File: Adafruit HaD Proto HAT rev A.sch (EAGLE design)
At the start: 9 parts, among them U1 CAT24C32

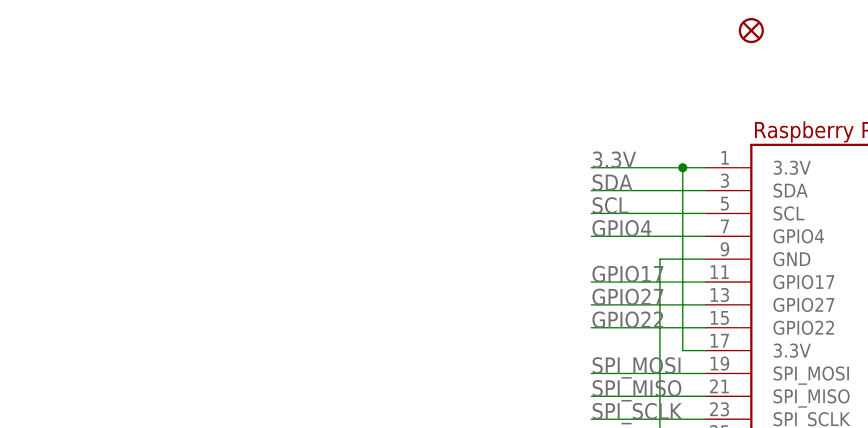
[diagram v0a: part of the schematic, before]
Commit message: ripped out proto area, added in 4xSAO connectors
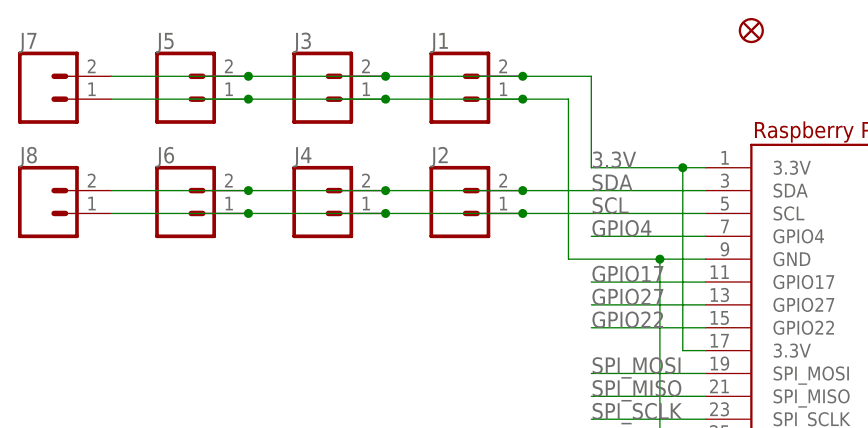
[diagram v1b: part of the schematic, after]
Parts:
- added J1, J2, J3, J4, J5, J6, J7, J8: (no value), SparkFun-Connectors:CONN_02LOCK
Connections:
- net 3.3V: now also J1.2, J3.2, J5.2, J7.2
- net GND: now also J1.1, J3.1, J5.1, J7.1
- net SCL: now also J2.1, J4.1, J6.1, J8.1
- net SDA: now also J2.2, J4.2, J6.2, J8.2
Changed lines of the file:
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@@
 <?xml version="1.0" encoding="utf-8"?>
 <!DOCTYPE eagle SYSTEM "eagle.dtd">
-<eagle version="6.3">
+<eagle version="9.0.1">
 <drawing>
 <settings>
 <setting alwaysvectorfont="no"/>
+<setting keepoldvectorfont="yes"/>
 <setting verticaltext="up"/>
 </settings>
@@
 <layer number="56" name="wert" color="7" fill="1" visible="no" active="no"/>
 <layer number="57" name="tCAD" color="7" fill="1" visible="no" active="no"/>
+<layer number="59" name="tCarbon" color="7" fill="1" visible="no" active="no"/>
+<layer number="60" name="bCarbon" color="7" fill="1" visible="no" active="no"/>
+<layer number="88" name="SimResults" color="9" fill="1" visible="no" active="yes"/>
+<layer number="89" name="SimProbes" color="9" fill="1" visible="no" active="yes"/>
+<layer number="90" name="Modules" color="5" fill="1" visible="yes" active="yes"/>
 <layer number="91" name="Nets" color="2" fill="1" visible="yes" active="yes"/>
 <layer number="92" name="Busses" color="1" fill="1" visible="yes" active="yes"/>
@@
 <layer number="97" name="Info" color="7" fill="1" visible="yes" active="yes"/>
 <layer number="98" name="Guide" color="6" fill="1" visible="yes" active="yes"/>
+<layer number="99" name="SpiceOrder" color="7" fill="1" visible="yes" active="yes"/>
 <layer number="100" name="Muster" color="7" fill="1" visible="no" active="yes"/>
 <layer number="101" name="Patch_Top" color="12" fill="4" visible="no" active="yes"/>
@@
 <layer number="111" name="MPL" color="7" fill="1" visible="no" active="yes"/>
 <layer number="112" name="tSilk" color="7" fill="1" visible="no" active="yes"/>
+<layer number="113" name="IDFDebug" color="4" fill="1" visible="no" active="no"/>
+<layer number="114" name="Badge_Outline" color="7" fill="1" visible="no" active="no"/>
+<layer number="115" name="ReferenceISLANDS" color="7" fill="1" visible="no" active="no"/>
 <layer number="116" name="Patch_BOT" color="9" fill="4" visible="no" active="yes"/>
+<layer number="118" name="Rect_Pads" color="7" fill="1" visible="no" active="no"/>
 <layer number="121" name="sName" color="7" fill="1" visible="no" active="yes"/>
 <layer number="122" name="_bPlace" color="7" fill="1" visible="no" active="yes"/>
@@
 <layer number="127" name="_tValues" color="7" fill="1" visible="no" active="yes"/>
 <layer number="128" name="_bValues" color="7" fill="1" visible="no" active="yes"/>
+<layer number="129" name="Mask" color="7" fill="1" visible="no" active="no"/>
 <layer number="131" name="tAdjust" color="7" fill="1" visible="no" active="yes"/>
 <layer number="132" name="bAdjust" color="7" fill="1" visible="no" active="yes"/>
@@
 <layer number="223" name="223bmp" color="24" fill="1" visible="no" active="no"/>
 <layer number="224" name="224bmp" color="25" fill="1" visible="no" active="no"/>
+<layer number="225" name="225bmp" color="7" fill="1" visible="no" active="no"/>
+<layer number="226" name="226bmp" color="7" fill="1" visible="no" active="no"/>
+<layer number="227" name="227bmp" color="7" fill="1" visible="no" active="no"/>
+<layer number="228" name="228bmp" color="7" fill="1" visible="no" active="no"/>
+<layer number="229" name="229bmp" color="7" fill="1" visible="no" active="no"/>
+<layer number="230" name="230bmp" color="7" fill="1" visible="no" active="no"/>
+<layer number="231" name="231bmp" color="7" fill="1" visible="no" active="no"/>
+<layer number="232" name="Eagle3D_PG2" color="7" fill="1" visible="no" active="no"/>
+<layer number="233" name="Eagle3D_PG3" color="7" fill="1" visible="no" active="no"/>
 <layer number="248" name="Housing" color="7" fill="1" visible="no" active="yes"/>
 <layer number="249" name="Edge" color="7" fill="1" visible="no" active="yes"/>
@@
 <layer number="251" name="SMDround" color="7" fill="1" visible="no" active="yes"/>
 <layer number="254" name="cooling" color="7" fill="1" visible="no" active="yes"/>
+<layer number="255" name="routoute" color="7" fill="1" visible="no" active="no"/>
 </layers>
 <schematic xreflabel="%N (%S.%C%R)" xrefpart="/%S.%C%R">
@@
 <part name="FID2" library="microbuilder" deviceset="FIDUCIAL" device="&quot;&quot;"/>
 <part name="FID3" library="microbuilder" deviceset="FIDUCIAL" device="&quot;&quot;"/>
+<part name="J1" library="SparkFun-Connectors" deviceset="CONN_02" device="LOCK"/>
+<part name="J2" library="SparkFun-Connectors" deviceset="CONN_02" device="LOCK"/>
+<part name="J3" library="SparkFun-Connectors" deviceset="CONN_02" device="LOCK"/>
+<part name="J4" library="SparkFun-Connectors" deviceset="CONN_02" device="LOCK"/>
+<part name="J5" library="SparkFun-Connectors" deviceset="CONN_02" device="LOCK"/>
+<part name="J6" library="SparkFun-Connectors" deviceset="CONN_02" device="LOCK"/>
+<part name="J7" library="SparkFun-Connectors" deviceset="CONN_02" device="LOCK"/>
+<part name="J8" library="SparkFun-Connectors" deviceset="CONN_02" device="LOCK"/>
 </parts>
 <sheets>
@@
 <instance part="FID2" gate="G$1" x="45.72" y="81.28"/>
 <instance part="FID3" gate="G$1" x="20.32" y="81.28"/>
+<instance part="J1" gate="G$1" x="-12.7" y="73.66"/>
+<instance part="J2" gate="G$1" x="-12.7" y="60.96"/>
+<instance part="J3" gate="G$1" x="-27.94" y="73.66"/>
+<instance part="J4" gate="G$1" x="-27.94" y="60.96"/>
+<instance part="J5" gate="G$1" x="-43.18" y="73.66"/>
+<instance part="J6" gate="G$1" x="-43.18" y="60.96"/>
+<instance part="J7" gate="G$1" x="-58.42" y="73.66"/>
+<instance part="J8" gate="G$1" x="-58.42" y="60.96"/>
 </instances>
 <busses>
@@
 <segment>
 <pinref part="RPI1" gate="G$1" pin="SDA"/>
-<wire x1="15.24" y1="63.5" x2="2.54" y2="63.5" width="0.1524" layer="91"/>
+<wire x1="15.24" y1="63.5" x2="-5.08" y2="63.5" width="0.1524" layer="91"/>
 <label x="2.54" y="63.5" size="1.778" layer="95"/>
+<pinref part="J2" gate="G$1" pin="2"/>
+<pinref part="J4" gate="G$1" pin="2"/>
+<wire x1="-5.08" y1="63.5" x2="-20.32" y2="63.5" width="0.1524" layer="91"/>
+<junction x="-5.08" y="63.5"/>
+<pinref part="J6" gate="G$1" pin="2"/>
+<wire x1="-20.32" y1="63.5" x2="-35.56" y2="63.5" width="0.1524" layer="91"/>
+<junction x="-20.32" y="63.5"/>
+<pinref part="J8" gate="G$1" pin="2"/>
+<wire x1="-35.56" y1="63.5" x2="-50.8" y2="63.5" width="0.1524" layer="91"/>
+<junction x="-35.56" y="63.5"/>
 </segment>
 <segment>
@@
 <segment>
 <pinref part="RPI1" gate="G$1" pin="SCL"/>
-<wire x1="15.24" y1="60.96" x2="2.54" y2="60.96" width="0.1524" layer="91"/>
+<wire x1="15.24" y1="60.96" x2="-5.08" y2="60.96" width="0.1524" layer="91"/>
 <label x="2.54" y="60.96" size="1.778" layer="95"/>
+<pinref part="J2" gate="G$1" pin="1"/>
+<pinref part="J4" gate="G$1" pin="1"/>
+<wire x1="-5.08" y1="60.96" x2="-20.32" y2="60.96" width="0.1524" layer="91"/>
+<junction x="-5.08" y="60.96"/>
+<pinref part="J6" gate="G$1" pin="1"/>
+<wire x1="-20.32" y1="60.96" x2="-35.56" y2="60.96" width="0.1524" layer="91"/>
+<junction x="-20.32" y="60.96"/>
+<pinref part="J8" gate="G$1" pin="1"/>
+<wire x1="-35.56" y1="60.96" x2="-50.8" y2="60.96" width="0.1524" layer="91"/>
+<junction x="-35.56" y="60.96"/>
 </segment>
 <segment>
@@
 <junction x="129.54" y="73.66"/>
 <label x="137.16" y="73.66" size="1.778" layer="95"/>
+<pinref part="J1" gate="G$1" pin="2"/>
+<wire x1="2.54" y1="66.04" x2="2.54" y2="76.2" width="0.1524" layer="91"/>
+<wire x1="2.54" y1="76.2" x2="-5.08" y2="76.2" width="0.1524" layer="91"/>
+<pinref part="J3" gate="G$1" pin="2"/>
+<wire x1="-5.08" y1="76.2" x2="-20.32" y2="76.2" width="0.1524" layer="91"/>
+<junction x="-5.08" y="76.2"/>
+<pinref part="J5" gate="G$1" pin="2"/>
+<wire x1="-20.32" y1="76.2" x2="-35.56" y2="76.2" width="0.1524" layer="91"/>
+<junction x="-20.32" y="76.2"/>
+<pinref part="J7" gate="G$1" pin="2"/>
+<wire x1="-35.56" y1="76.2" x2="-50.8" y2="76.2" width="0.1524" layer="91"/>
+<junction x="-35.56" y="76.2"/>
 </segment>
 <segment>
@@
 <junction x="10.16" y="35.56"/>
 <pinref part="RPI1" gate="G$1" pin="GND@5"/>
-</segment>
-<segment>
+<wire x1="10.16" y1="55.88" x2="0" y2="55.88" width="0.1524" layer="91"/>
+<junction x="10.16" y="55.88"/>
+<pinref part="J1" gate="G$1" pin="1"/>
+<wire x1="0" y1="55.88" x2="0" y2="73.66" width="0.1524" layer="91"/>
+<wire x1="0" y1="73.66" x2="-5.08" y2="73.66" width="0.1524" layer="91"/>
+<pinref part="J3" gate="G$1" pin="1"/>
+<wire x1="-5.08" y1="73.66" x2="-20.32" y2="73.66" width="0.1524" layer="91"/>
+<junction x="-5.08" y="73.66"/>
+<pinref part="J5" gate="G$1" pin="1"/>
+<wire x1="-20.32" y1="73.66" x2="-35.56" y2="73.66" width="0.1524" layer="91"/>
+<junction x="-20.32" y="73.66"/>
+<pinref part="J7" gate="G$1" pin="1"/>
+<wire x1="-35.56" y1="73.66" x2="-50.8" y2="73.66" width="0.1524" layer="91"/>
+<junction x="-35.56" y="73.66"/>
+</segment>
+<segment>
